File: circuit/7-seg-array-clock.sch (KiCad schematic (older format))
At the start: 2 parts

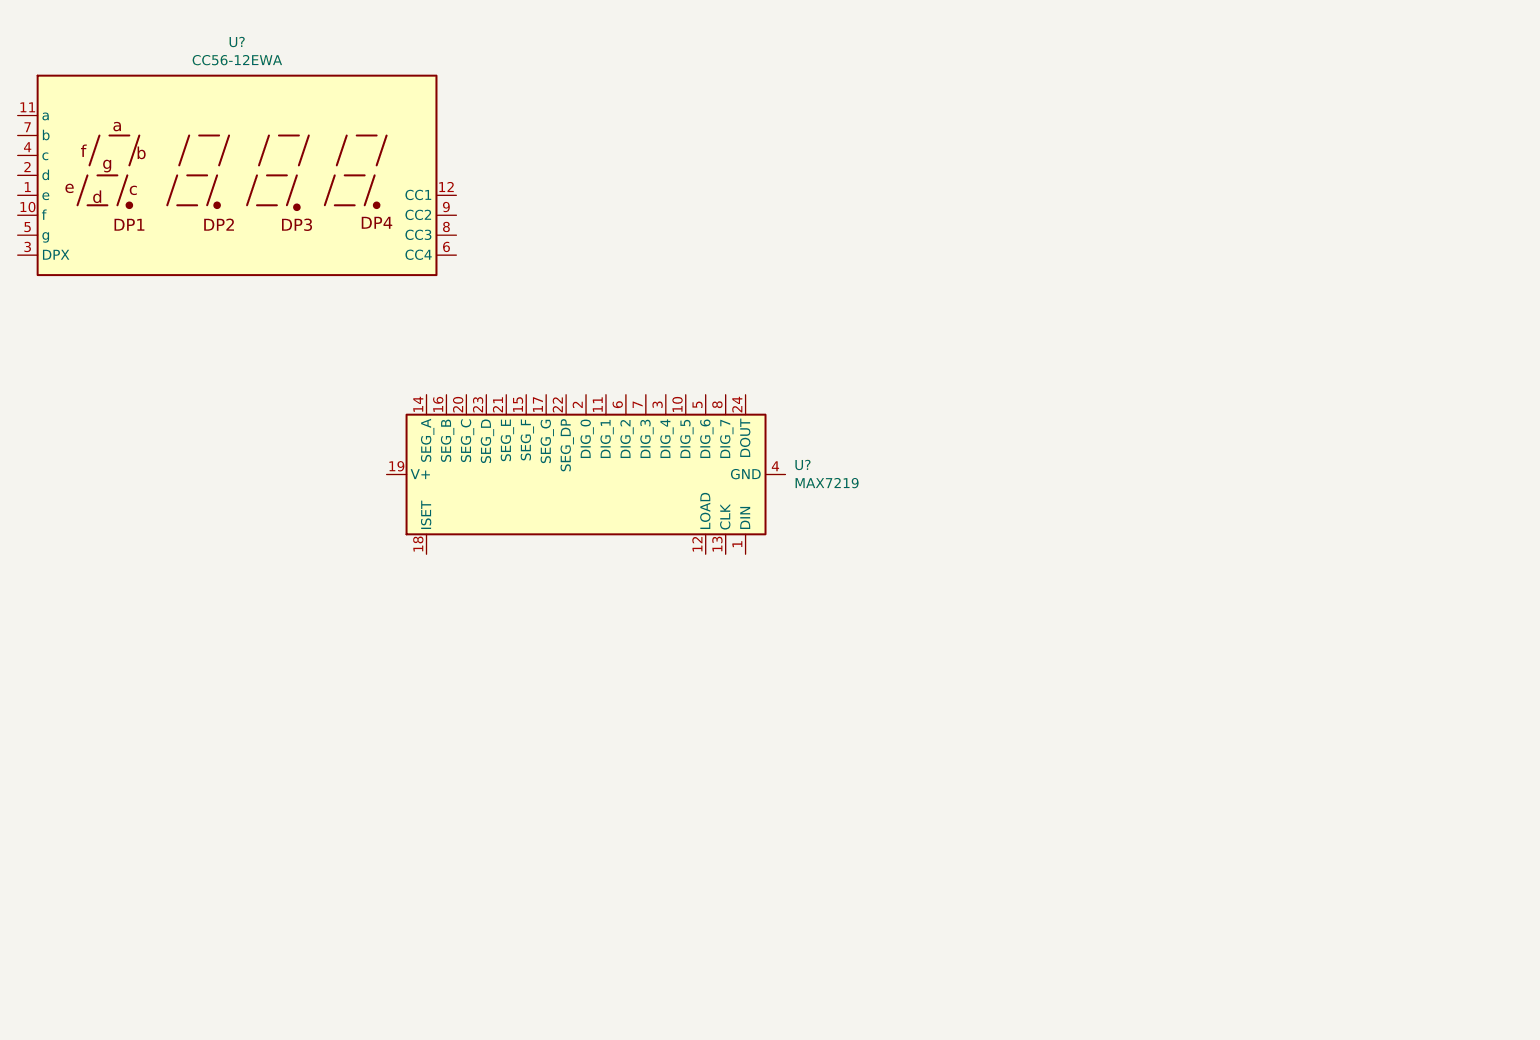
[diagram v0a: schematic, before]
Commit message: Completed display circuit and made basic PCB layout
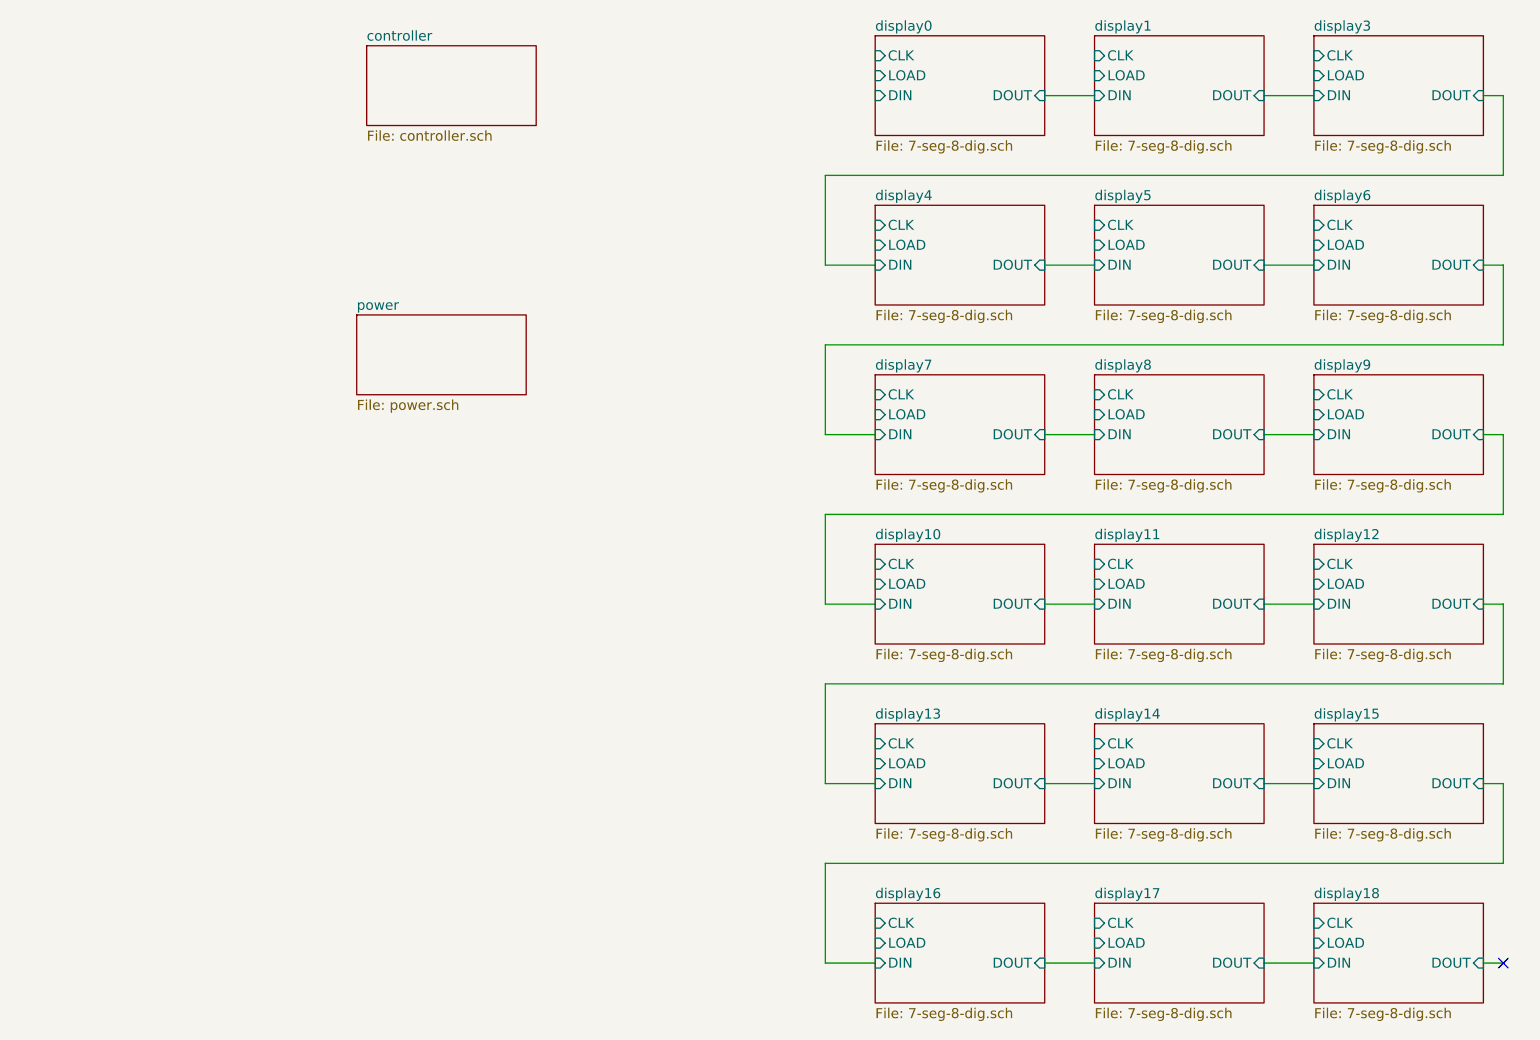
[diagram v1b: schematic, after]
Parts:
- removed U?: CC56-12EWA, Display_7Segment:CA56-12EWA, symbol Display_Character:CC56-12EWA
- removed U?: MAX7219, symbol Driver_LED:MAX7219
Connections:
- no-connect marks 0 -> 1

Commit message: Added microcontroller circuit
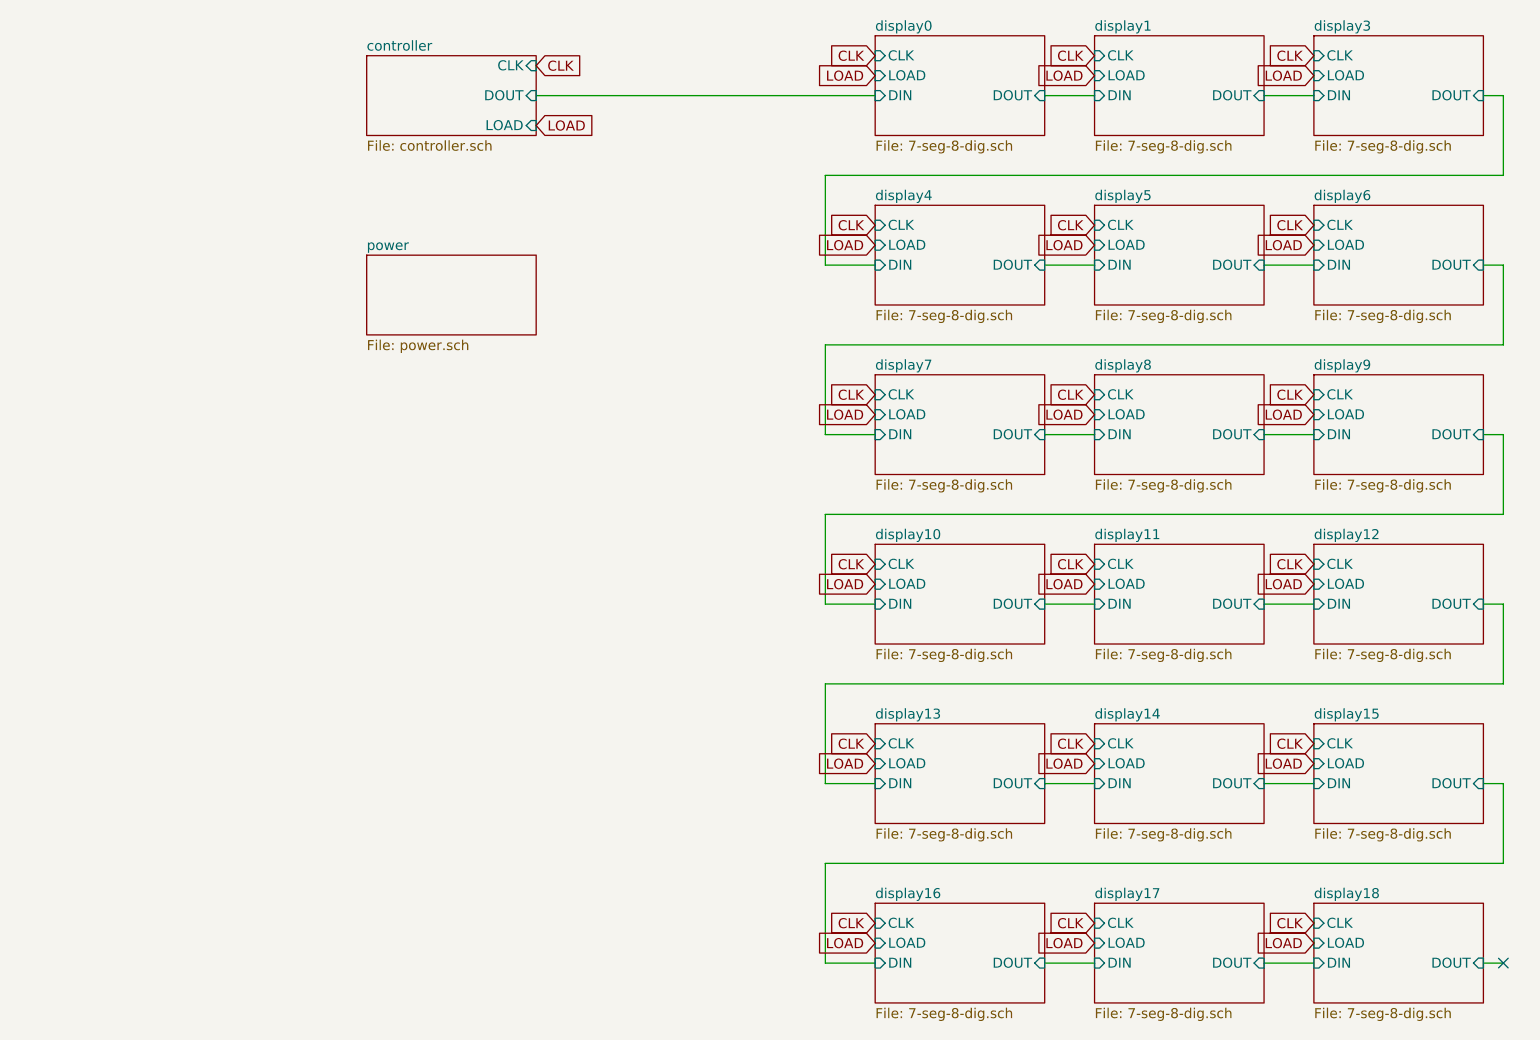
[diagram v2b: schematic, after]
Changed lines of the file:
@@
 $EndSheet
 $Sheet
-S 2900 1100 850  400
-U 5E35994B
-F0 "controller" 50
-F1 "controller.sch" 50
-$EndSheet
-$Sheet
-S 2850 2450 850  400
+S 2900 2150 850  400
 U 5E359990
 F0 "power" 50
@@
 Wire Wire Line
 	8600 5700 8500 5700
+Wire Wire Line
+	3750 1350 5450 1350
+$Sheet
+S 2900 1150 850  400
+U 5E35994B
+F0 "controller" 50
+F1 "controller.sch" 50
+F2 "DOUT" I R 3750 1350 50
+F3 "CLK" I R 3750 1200 50
+F4 "LOAD" I R 3750 1500 50
+$EndSheet
+Text GLabel 5450 1250 0    50   Input ~ 0
+LOAD
+Text GLabel 6550 1250 0    50   Input ~ 0
+LOAD
+Text GLabel 7650 1250 0    50   Input ~ 0
+LOAD
+Text GLabel 7650 2100 0    50   Input ~ 0
+LOAD
+Text GLabel 6550 2100 0    50   Input ~ 0
+LOAD
+Text GLabel 5450 2100 0    50   Input ~ 0
+LOAD
+Text GLabel 7650 2950 0    50   Input ~ 0
+LOAD
+Text GLabel 6550 2950 0    50   Input ~ 0
+LOAD
+Text GLabel 5450 2950 0    50   Input ~ 0
+LOAD
+Text GLabel 5450 3800 0    50   Input ~ 0
+LOAD
+Text GLabel 6550 3800 0    50   Input ~ 0
+LOAD
+Text GLabel 7650 3800 0    50   Input ~ 0
+LOAD
+Text GLabel 7650 4700 0    50   Input ~ 0
+LOAD
+Text GLabel 6550 4700 0    50   Input ~ 0
+LOAD
+Text GLabel 5450 4700 0    50   Input ~ 0
+LOAD
+Text GLabel 5450 5600 0    50   Input ~ 0
+LOAD
+Text GLabel 6550 5600 0    50   Input ~ 0
+LOAD
+Text GLabel 7650 5600 0    50   Input ~ 0
+LOAD
+Text GLabel 3750 1500 2    50   Input ~ 0
+LOAD
+Text GLabel 3750 1200 2    50   Input ~ 0
+CLK
+Text GLabel 5450 1150 0    50   Input ~ 0
+CLK
+Text GLabel 6550 1150 0    50   Input ~ 0
+CLK
+Text GLabel 7650 1150 0    50   Input ~ 0
+CLK
+Text GLabel 5450 2000 0    50   Input ~ 0
+CLK
+Text GLabel 6550 2000 0    50   Input ~ 0
+CLK
+Text GLabel 7650 2000 0    50   Input ~ 0
+CLK
+Text GLabel 7650 2850 0    50   Input ~ 0
+CLK
+Text GLabel 6550 2850 0    50   Input ~ 0
+CLK
+Text GLabel 5450 2850 0    50   Input ~ 0
+CLK
+Text GLabel 5450 3700 0    50   Input ~ 0
+CLK
+Text GLabel 6550 3700 0    50   Input ~ 0
+CLK
+Text GLabel 7650 3700 0    50   Input ~ 0
+CLK
+Text GLabel 7650 4600 0    50   Input ~ 0
+CLK
+Text GLabel 6550 4600 0    50   Input ~ 0
+CLK
+Text GLabel 5450 4600 0    50   Input ~ 0
+CLK
+Text GLabel 5450 5500 0    50   Input ~ 0
+CLK
+Text GLabel 6550 5500 0    50   Input ~ 0
+CLK
+Text GLabel 7650 5500 0    50   Input ~ 0
+CLK
 $EndSCHEMATC
